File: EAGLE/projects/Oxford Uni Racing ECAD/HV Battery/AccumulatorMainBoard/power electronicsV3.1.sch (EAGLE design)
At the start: 97 parts, among them IC1 4043D, IC2 SE555D, IC3 4011D, IC5 4043D, IC6 4011D, IC7 4011D, IC8 4011D, IC9 4011D, K1 T9AS1D12-48=T9A, K2 T9AS5D12-12=T9A, K3 T9AS1D12-48=T9A, K4 T9AS1D12-48=T9A, Q1 BSS138, Q2 BSS138, Q3 BSS138, Q4 BSS138

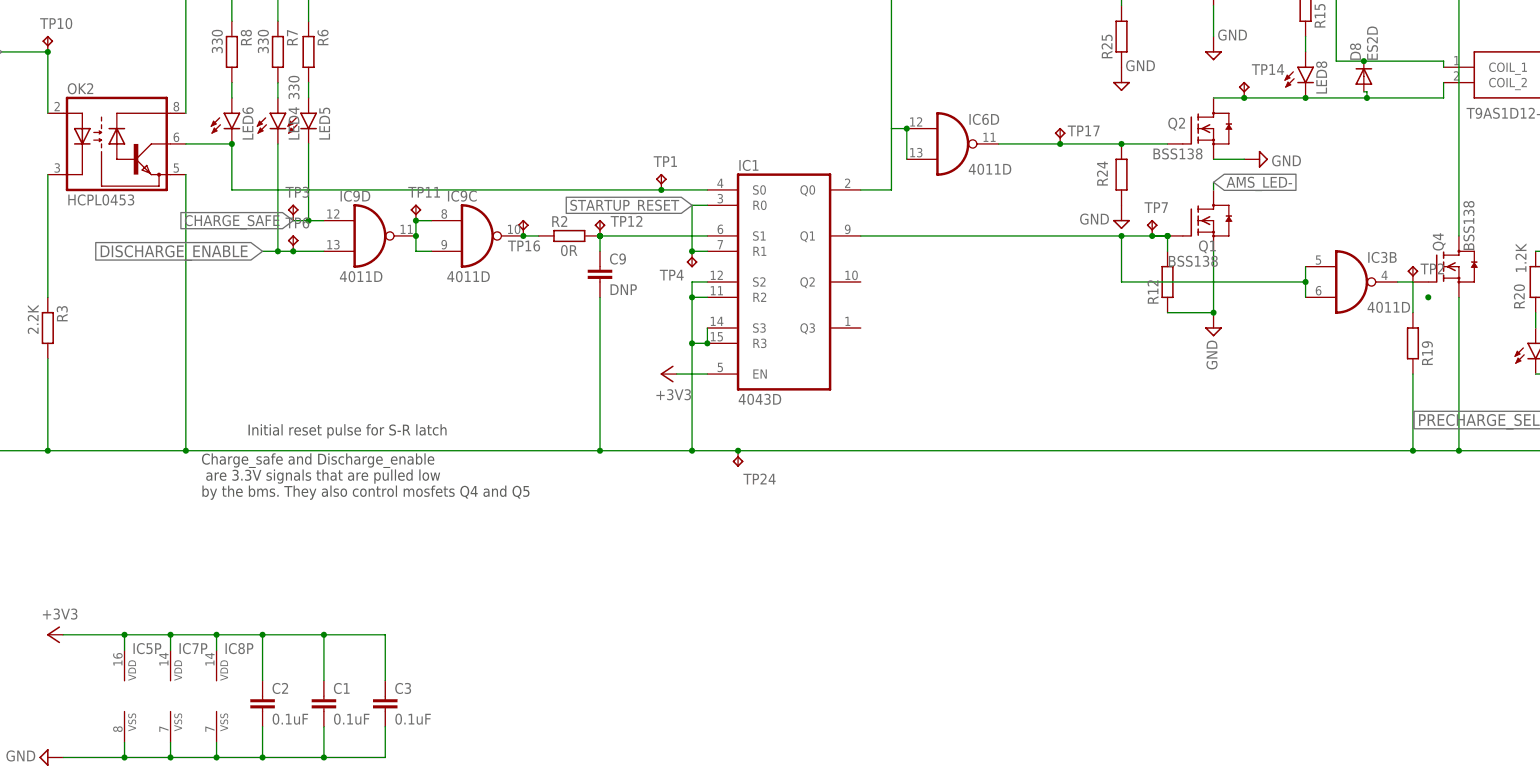
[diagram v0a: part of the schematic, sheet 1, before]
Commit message: Main Board V4.1
Moves some of the IC to the bottom layer. More optimal Connector placement
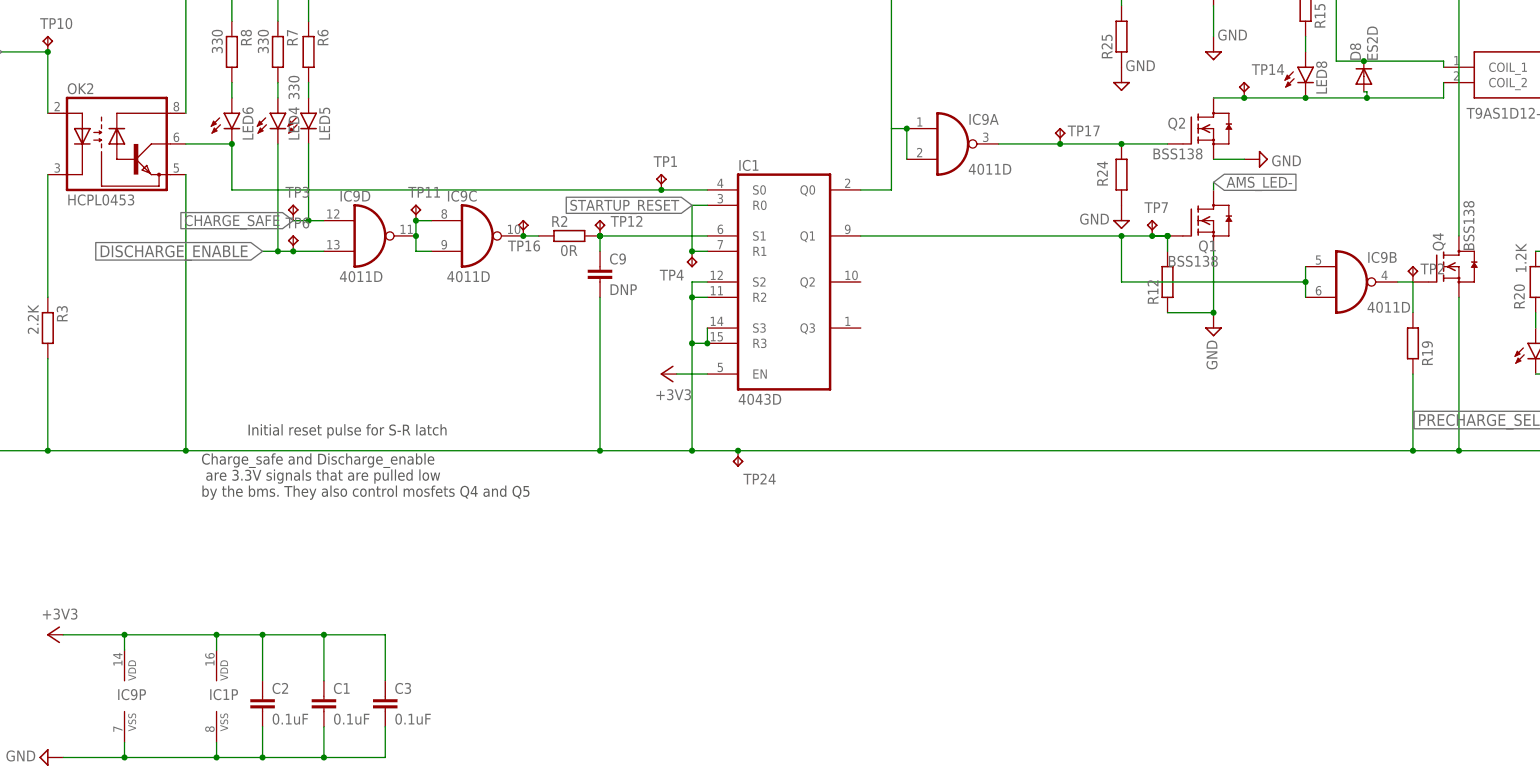
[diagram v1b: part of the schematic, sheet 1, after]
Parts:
- removed IC3, IC6, IC7, IC8: 4011D, 40xx:4011D
- removed IC5: 4043D, 40xx:4043D
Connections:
- net +3V3: now also IC1P.VDD, IC9P.VDD; no longer IC5P.VDD, IC7P.VDD, IC8P.VDD
- net DISCHARGE_ENABLE: now also IC9B.I0, IC9B.I1; no longer IC3B.I0, IC3B.I1
- net GND: now also IC1P.VSS, IC9P.VSS; no longer IC5P.VSS, IC7P.VSS, IC8P.VSS
- net N$16: now also IC9B.O; no longer IC3B.O
- net N$8: now also IC9A.O; no longer IC6D.O
- net N$9: now also IC9A.I0, IC9A.I1; no longer IC6D.I0, IC6D.I1
